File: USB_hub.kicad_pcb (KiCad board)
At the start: 6 copper layers, 121.3 x 91.8 mm, 310 parts, among them J1 USB_SPI_(Opt), J10 USB3_A, J11 8-pin ATX connector, J12 USB_C_Receptacle, J13 I2C_HD3SS3220, J2 USB_C_Receptacle, J3 I2C_HD3SS3220, J4 USB_C_Receptacle, J5 I2C2_PD_Controller, J6 I2C_Mux, J7 I2C_EEPROM, J8 SD_Card_Receptacle, J9 USB3_A, Q1 MMBT2222A, SW1 RESET_HUB, SW2 FW_Upgrade, U1 USB7206C/KDX, U10 24LC256, U11 TPD4E02B04DQA, U12 TPD4E02B04DQA, U13 TPD4E02B04DQA, U14 TUSB1142IRNQR_C5216209, U15 GL3224-OIY04, U16 TPD4E02B04DQA, U17 TPD4E02B04DQA, U18 UCS2114-1-V/G4, U19 TPD4E02B04DQA, U2 MIC803-29D4VM3-TR, U20 TPD4E02B04DQA, U21 SiRA80DP, U22 TPS25983, U23 AP7361C-33ER, U24 MP8795, U25 MIC23201YML-TR, U26 HD3SS3220IRNHR, U27 TPD4E02B04DQA, U28 TPD4E02B04DQA, U29 TPD4E02B04DQA, U3 HD3SS3220IRNHR, U32 TPD4E02B04DQA, U4 TPS2068EDBVR, U5 TPD4E02B04DQA, U6 TPD4E02B04DQA, U7 TPD4E02B04DQA, U8 TVS2200DRV, U9 TPS25762CQRQLRQ1, Y1 25MHz, Y2 25MHz +-0.03%

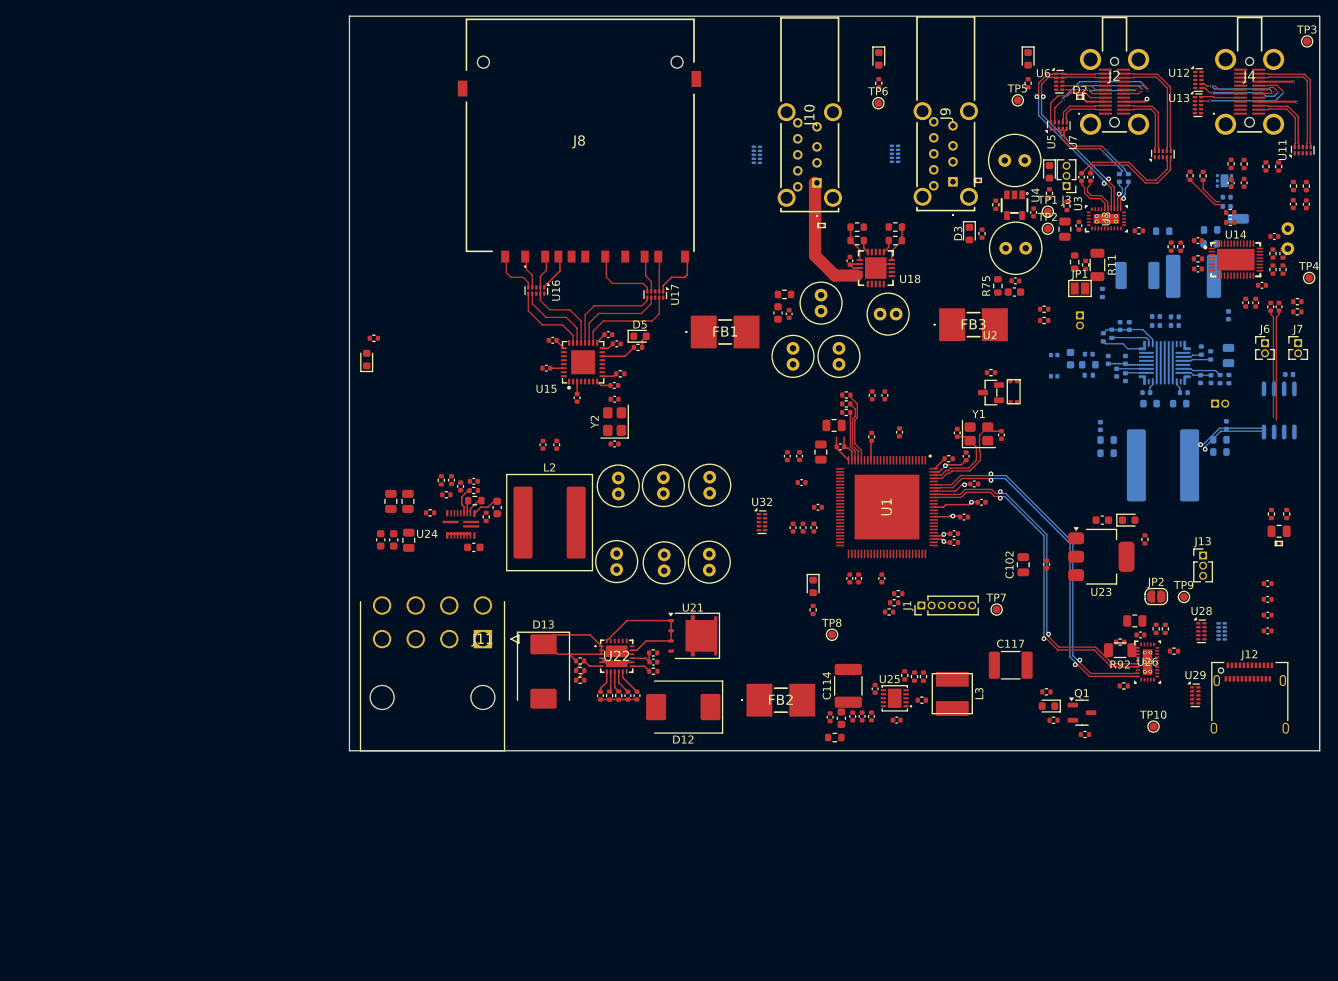
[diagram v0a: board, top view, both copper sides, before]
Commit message: AP7361C'sOO footprint changed, Inductors footprint improved
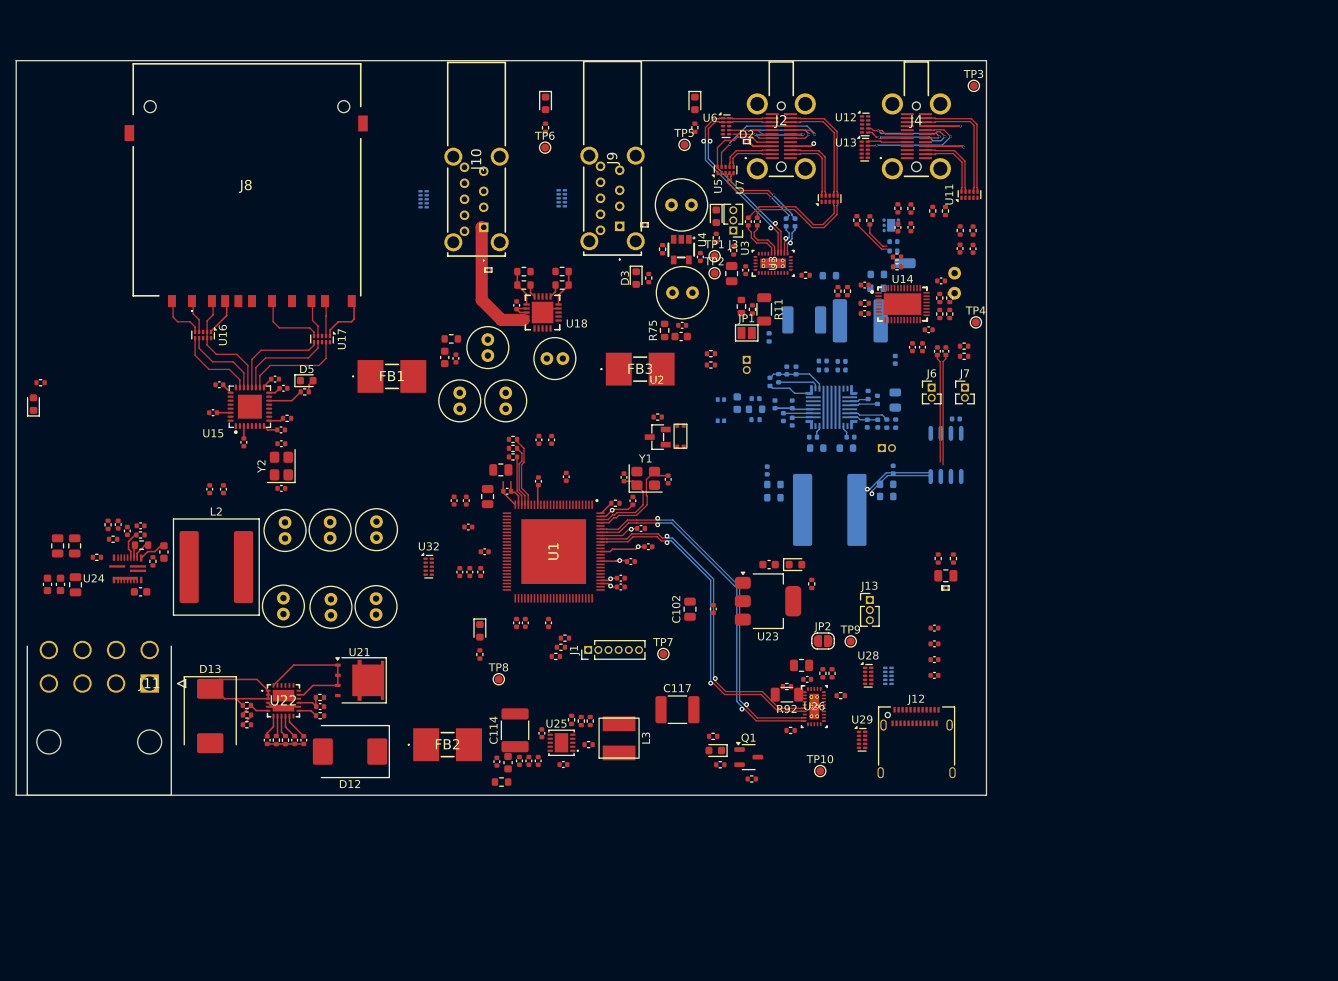
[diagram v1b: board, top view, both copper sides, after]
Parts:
- L1, L2: footprint Inductor_SMD:L_Coilcraft_XAL1010-XXX -> Inductor_SMD:L_YSPIT1010A
- moved J5 42.0 mm to (116.4, 58.5)
- moved TP5 42.0 mm to (108.7, 31.6)
- moved C1 42.0 mm to (86.5, 74.9)
- moved C100 42.0 mm to (29.0, 86.5)
- moved C101 42.0 mm to (119.2, 84.1)
- moved C102 42.0 mm to (109.3, 89.6)
- moved C106 42.0 mm to (64.5, 88.4)
- moved C109 42.0 mm to (70.2, 80.7)
- moved C110 42.0 mm to (70.1, 88.3)
- moved C114 42.0 mm to (87.5, 104.8)
- moved C115 42.0 mm to (90.4, 108.6)
- moved C119 42.0 mm to (89.2, 108.6)
- moved C12 42.0 mm to (81.8, 85.0)
- moved C120 42.0 mm to (90.8, 105.2)
- moved C122 42.0 mm to (124.0, 98.4)
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
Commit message: Rearrange of the component placement, scheme changes for better routing
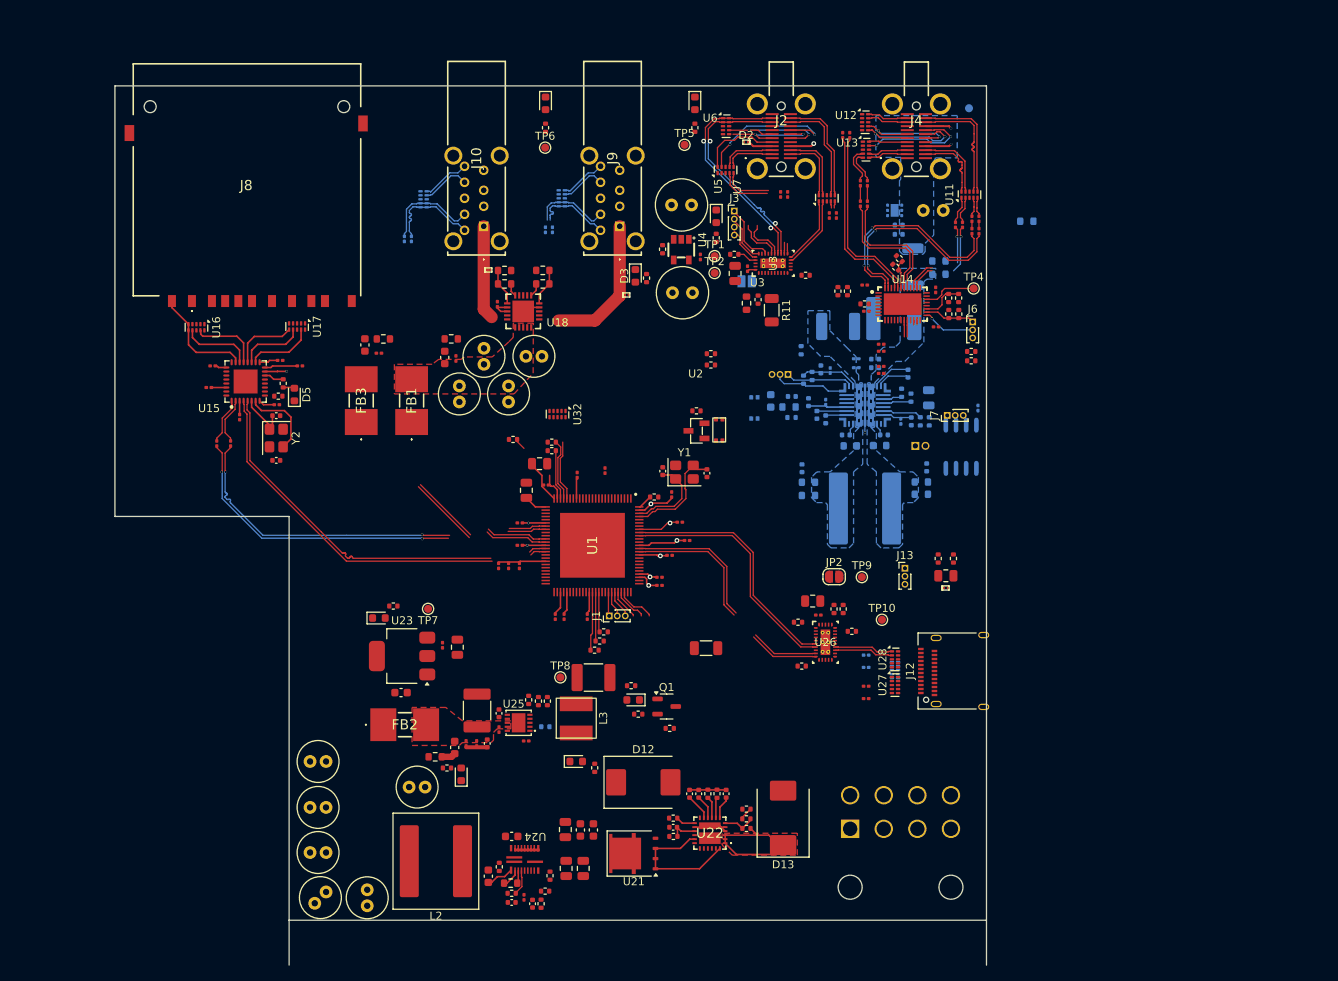
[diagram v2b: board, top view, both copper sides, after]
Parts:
- C1, C103, C11, C112, C115, C116, C118, C12, C122, C123, C124, C13, C14, C15, C16, C17, C18, C2, C24, C27, C28, C3, C30, C33, C35, C37, C39, C4, C40, C5, C56, C6, C61, C62, C63, C64, C66, C67, C68, C69, C7, C70, C71, C72, C73, C74, C75, C76, C77, C8, C84, C86, C9, C92, C94: footprint Capacitor_SMD:C_0402_1005Metric -> Capacitor_SMD:C_0201_0603Metric
- C125, C126, C127, C128, C129, C130: footprint Capacitor_SMD:C_0402_1005Metric -> Capacitor_SMD:C_0201_0603Metric; moved to B.Cu
- C25, C26: footprint Capacitor_SMD:C_0402_1005Metric -> Capacitor_SMD:C_0201_0603Metric; moved to F.Cu
- C57, C58, C59, C60: value 330nF -> 220nF; footprint Capacitor_SMD:C_0402_1005Metric -> Capacitor_SMD:C_0201_0603Metric
- J1: footprint Connector_PinHeader_1.27mm:PinHeader_1x06_P1.27mm_Vertical -> Connector_PinHeader_1.00mm:PinHeader_1x03_P1.00mm_Vertical
- J11, JP1, R88, TP3, U29: moved to B.Cu
- J13: footprint Connector_PinHeader_1.27mm:PinHeader_1x03_P1.27mm_Vertical -> Connector_PinHeader_1.00mm:PinHeader_1x03_P1.00mm_Vertical
- J3: footprint Connector_PinHeader_1.27mm:PinHeader_1x03_P1.27mm_Vertical -> Connector_PinHeader_1.00mm:PinHeader_1x04_P1.00mm_Vertical
- J5, J6, J7: footprint Connector_PinHeader_1.27mm:PinHeader_1x02_P1.27mm_Vertical -> Connector_PinHeader_1.00mm:PinHeader_1x03_P1.00mm_Vertical
- L1, L2: footprint Inductor_SMD:L_YSPIT1010A -> Inductor_SMD:L_Coilcraft_XAL1010-XXX
- R41, R42, R44, R47, R48, R49, R52, R53: footprint Resistor_SMD:R_0402_1005Metric -> Resistor_SMD:R_0201_0603Metric
- U23: value AP7361C-33ER -> AP7361C-33E
- U27: moved to F.Cu
- moved J11 89.4 mm to (129.4, 117.1), turned to 180 degrees
- moved C96 77.1 mm to (96.0, 122.1), turned to -90 degrees
- moved C100 74.8 mm to (97.3, 117.2), turned to 90 degrees
- moved C98 73.5 mm to (93.9, 122.1), turned to -90 degrees
- moved D13 72.7 mm to (121.0, 115.7), turned to 90 degrees
- moved R78 71.9 mm to (90.7, 126.5), turned to -90 degrees
- moved C99 71.9 mm to (95.6, 117.2), turned to 90 degrees
- moved D16 70.7 mm to (80.7, 110.3)
- moved C104 70.2 mm to (89.7, 126.5), turned to -90 degrees
- moved R85 70.0 mm to (79.0, 109.5), turned to 0 degrees
- moved R79 69.6 mm to (91.2, 124.9)
- moved R77 69.2 mm to (91.8, 123.0), turned to 90 degrees
- moved C97 68.4 mm to (93.8, 117.2), turned to 90 degrees
- moved C112 67.5 mm to (88.6, 125.7), turned to -90 degrees
- moved C113 66.1 mm to (87.1, 126.3), turned to 180 degrees
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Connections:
- net Net-(U1-USB3DN_TXDM2) renamed /USB7206C/DN2TX-
- net Net-(U1-USB3DN_TXDM3) renamed /USB7206C/DN3TX-
- net Net-(U1-USB3DN_TXDP2) renamed /USB7206C/DN2TX+
- net Net-(U1-USB3DN_TXDP3) renamed /USB7206C/DN3TX+
- net Net-(U14-SSRXn) renamed /USB-C2/RX1-
- net Net-(U14-SSRXp) renamed /USB-C2/RX1+
- net Net-(U14-SSTXn) renamed /USB-C2/TX1-
- net Net-(U14-SSTXp) renamed /USB-C2/TX1+
- net Net-(U15-TXN) renamed /SD-interface/TX1-
- net Net-(U15-TXP) renamed /SD-interface/TX1+
- C123 pad 2: /USB-C_UP1/USB-C1.TX1+ -> unconnected-(C123-Pad2)
- C124 pad 2: /USB-C_UP1/USB-C1.TX1- -> /USB-C_UP1/USB-C1.TX1+
- C127 pad 2: /USB-A1/USB-A1.TX1+ -> /USB-A1/USB-A2.TX1+
- C128 pad 2: /USB-A1/USB-A1.TX1- -> /USB-A1/USB-A2.TX1-
- C129 pad 2: /USB-A1/USB-A2.TX1+ -> /USB-A1/USB-A1.TX1+
- C130 pad 2: /USB-A1/USB-A2.TX1- -> /USB-A1/USB-A1.TX1-
- J3 pad 1: /USB-C1/I2C_HD3SS3220.SDA -> GND
- J3 pad 3: /USB-C1/I2C_HD3SS3220.INT_N -> /USB-C1/I2C_HD3SS3220.SDA
- J4 pad A1: GND -> PGND
- J4 pad A12: GND -> PGND
- J4 pad B1: GND -> PGND
- J4 pad B12: GND -> PGND
- J4 pad B2: /USB-C2/USB-C2.TX2+ -> /USB-C2/USB-C2.TX2-
- J4 pad B3: /USB-C2/USB-C2.TX2- -> /USB-C2/USB-C2.TX2+
- R41 pad 2: /USB-C2/USB-C2.TX2+ -> /USB-C2/USB-C2.TX2-
- R42 pad 2: /USB-C2/USB-C2.TX2- -> /USB-C2/USB-C2.TX2+
- U1 pad 14: /USB-A1/USB-A2.D+ -> /USB-A1/USB-A1.D+
- U1 pad 15: /USB-A1/USB-A2.D- -> /USB-A1/USB-A1.D-
- U1 pad 19: /USB-A1/USB-A2.RX1+ -> /USB-A1/USB-A1.RX1+
- U1 pad 20: /USB-A1/USB-A2.RX1- -> /USB-A1/USB-A1.RX1-
- U1 pad 27: /USB-A1/USB-A1.D+ -> /USB-A1/USB-A2.D+
- U1 pad 28: /USB-A1/USB-A1.D- -> /USB-A1/USB-A2.D-
- U1 pad 32: /USB-A1/USB-A1.RX1+ -> /USB-A1/USB-A2.RX1+
- U1 pad 33: /USB-A1/USB-A1.RX1- -> /USB-A1/USB-A2.RX1-
- U11 pad 4: /USB-C2/USB-C2.TX2- -> /USB-C2/USB-C2.TX2+
- U11 pad 5: /USB-C2/USB-C2.TX2+ -> /USB-C2/USB-C2.TX2-
- U11 pad 6: /USB-C2/USB-C2.TX2+ -> /USB-C2/USB-C2.TX2-
- U11 pad 7: /USB-C2/USB-C2.TX2- -> /USB-C2/USB-C2.TX2+
- U14 pad 33: /USB-C2/CTX1- -> /USB-C2/CTX1+
- U14 pad 34: /USB-C2/CTX1+ -> /USB-C2/CTX1-
- U14 pad 39: /USB-C2/CTX2- -> /USB-C2/CTX2+
- U14 pad 40: /USB-C2/CTX2+ -> /USB-C2/CTX2-
- U15 pad 15: +5V -> +5V_USB_C_SD
- U23 pad 1: GND -> +5V_Power
- U23 pad 2: +3V3 -> GND
- U23 pad 3: +5V_Power -> +3V3
- U27 pad 4: /USB-C_UP1/USB-C1.D- -> /USB-C_UP1/USB-C1.TX1-
- U27 pad 5: /USB-C_UP1/USB-C1.D+ -> /USB-C_UP1/USB-C1.TX1+
- U27 pad 6: /USB-C_UP1/USB-C1.D+ -> /USB-C_UP1/USB-C1.TX1+
- U27 pad 7: /USB-C_UP1/USB-C1.D- -> /USB-C_UP1/USB-C1.TX1-
- U28 pad 4: /USB-C_UP1/USB-C1.TX1- -> /USB-C_UP1/USB3_IN.D-
- U28 pad 5: /USB-C_UP1/USB-C1.TX1+ -> /USB-C_UP1/USB3_IN.D+
- U28 pad 6: /USB-C_UP1/USB-C1.TX1+ -> /USB-C_UP1/USB3_IN.D+
- U28 pad 7: /USB-C_UP1/USB-C1.TX1- -> /USB-C_UP1/USB3_IN.D-
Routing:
- net /SD-interface/USB-SD.RX1-: track 0.00 -> 45.6 mm
- net /SD-interface/USB-SD.RX1+: track 0.00 -> 45.6 mm
- net /SD-interface/USB-SD.TX1-: track 0.00 -> 45.0 mm, vias 0 -> 2
- net /SD-interface/USB-SD.TX1+: track 0.00 -> 45.0 mm, vias 0 -> 2
- net /USB-C_UP1/USB3_IN.RX1+: track 44.9 -> 8.50 mm, vias 2 -> 0
- net /USB-C_UP1/USB3_IN.RX1-: track 44.9 -> 8.80 mm, vias 2 -> 0
- net /USB-C2/CTX2-: track 0.00 -> 26.9 mm, vias 0 -> 2
- net /USB-C2/CTX2+: track 0.00 -> 26.9 mm, vias 0 -> 2
- net /USB-A1/USB-A2.RX1-: track 0.00 -> 19.9 mm
- net /USB-A1/USB-A2.RX1+: track 0.00 -> 19.6 mm
- net /USB-C2/CRX2-: track 3.89 -> 22.8 mm
- net /USB-C2/CRX2+: track 5.04 -> 22.8 mm
- net VBUS-A1: track 0.00 -> 17.6 mm
- net /USB-C2/CTX1-: track 0.00 -> 15.8 mm
- net /USB-C2/CTX1+: track 0.00 -> 15.8 mm
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- added copper zone on F.Cu, net +5V_Power
- added copper zone on F.Cu, net +5V_USB_A
- added copper zone on F.Cu, net Net-(D13-C)
- added copper zone on B.Cu, net Net-(U9-OUT)
- added copper zone on B.Cu, net Net-(U9-SW1)
- added copper zone on B.Cu, net Net-(U9-SW2)
- added copper zone on B.Cu, net VBUS
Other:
- board size 121.3 x 91.8 mm -> 108.9 x 109.9 mm

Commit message: board outline repaired, 3d model and schematic exported
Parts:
- moved J12 0.73 mm to (142.5, 97.2)
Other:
- board size 108.9 x 109.9 mm -> 108.9 x 104.3 mm
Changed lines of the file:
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@@
 	(footprint "Connector_USB:USB_C_Receptacle_Amphenol_12401610E4-2A"
 		(layer "F.Cu")
-		(at 143.2232 97.369 90)
+		(at 142.5194 97.1804 90)
 		(descr "USB TYPE C, RA RCPT PCB, SMT, https://www.amphenolcanada.com/StockAvailabilityPrice.aspx?From=&PartNum=12401610E4%7e2A")
 		(tags "USB C Type-C Receptacle SMD")
@@
 			(size 0.85 0.85)
 			(drill 0.5)
-			(layers "F&B.Cu" "*.Mask")
+			(layers "*.Cu" "*.Mask")
 			(remove_unused_layers no)
 			(net 84 "/USB-C2/I2C2_TPS.SDA")
@@
 			(size 0.85 0.85)
 			(drill 0.5)
-			(layers "F&B.Cu" "*.Mask")
+			(layers "*.Cu" "*.Mask")
 			(remove_unused_layers no)
 			(net 83 "/USB-C2/I2C2_TPS.SCL")
@@
 			(size 0.85 0.85)
 			(drill 0.5)
-			(layers "F&B.Cu" "*.Mask")
+			(layers "*.Cu" "*.Mask")
 			(remove_unused_layers no)
 			(net 1 "GND")
@@
 			(size 1.6 1.6)
 			(drill 0.8)
-			(layers "F&B.Cu" "*.Mask")
+			(layers "*.Cu" "*.Mask")
 			(remove_unused_layers no)
 			(net 25 "VBUS")
@@
 			(size 1.6 1.6)
 			(drill 0.8)
-			(layers "F&B.Cu" "*.Mask")
+			(layers "*.Cu" "*.Mask")
 			(remove_unused_layers no)
 			(net 12 "PGND")
@@
 	(gr_line
 		(start 146.4056 24.2316)
-		(end 146.4056 134.1374)
+		(end 146.4056 128.524)
 		(stroke
 			(width 0.05)
@@
 	)
 	(gr_line
-		(start 146.3802 128.524)
-		(end 59.2074 128.524)
+		(start 146.4056 128.524)
+		(end 59.2328 128.524)
 		(stroke
 			(width 0.05)
@@
 	(gr_line
 		(start 59.2328 78.0542)
-		(end 59.2328 134.1374)
+		(end 59.2328 128.524)
 		(stroke
 			(width 0.05)
@@
 				(xy 124.079414 56.445512) (xy 124.079414 52.330712) (xy 126.822614 52.330712) (xy 126.822614 52.762512)
 				(xy 126.8222 52.7812) (xy 126.822614 52.813312) (xy 126.822614 54.819912) (xy 128.905414 56.902712)
-				(xy 128.905414 56.902712) (xy 130.124614 58.121912) (xy 130.124614 60.058662) (xy 130.429 60.325)
-				(xy 130.441826 66.836339)
+				(xy 130.124614 58.121912) (xy 130.124614 60.058662) (xy 130.429 60.325) (xy 130.441826 66.836339)
 			)
 		)
